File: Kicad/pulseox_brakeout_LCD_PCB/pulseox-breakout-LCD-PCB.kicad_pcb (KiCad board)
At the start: 2 copper layers, 47.4 x 44.4 mm, 20 parts, among them CON1 P3, P1 Header 8, P2 Header 2

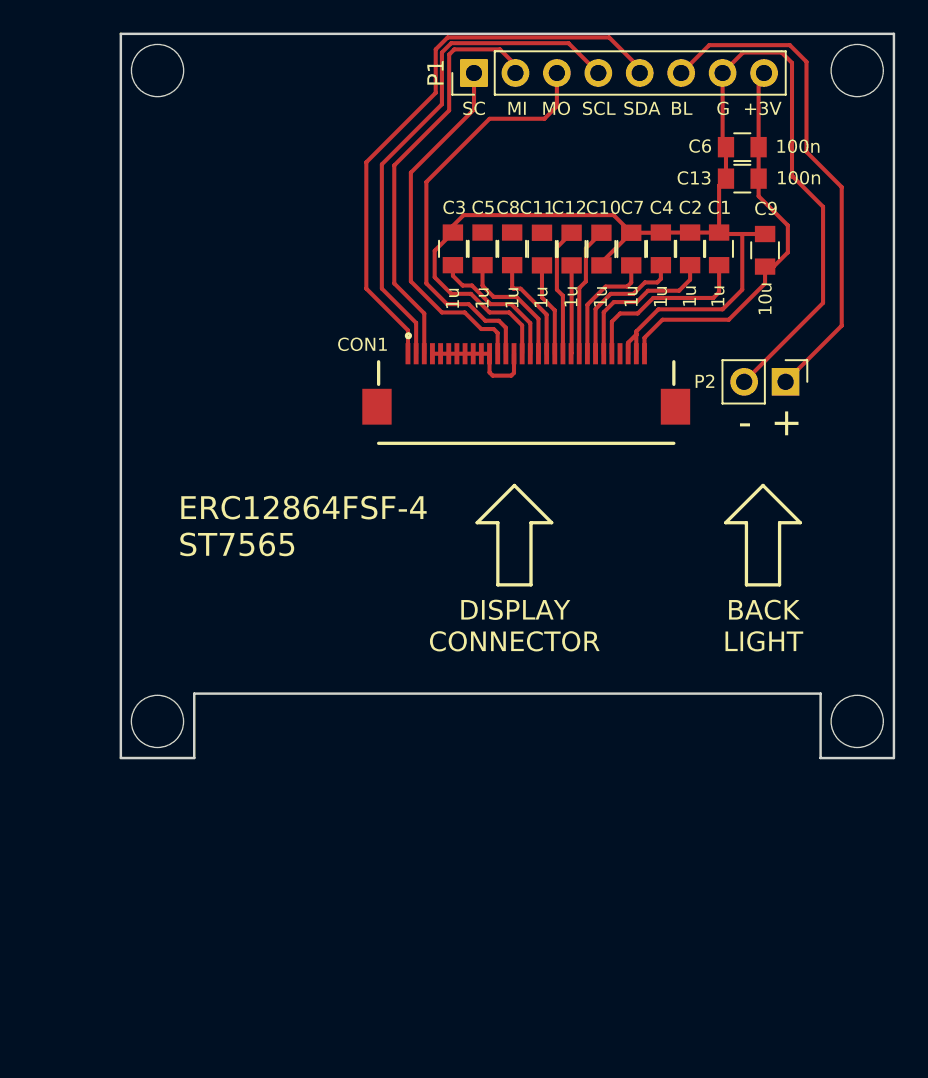
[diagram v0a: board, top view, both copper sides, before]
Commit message: Added output PDF files from Kicad project
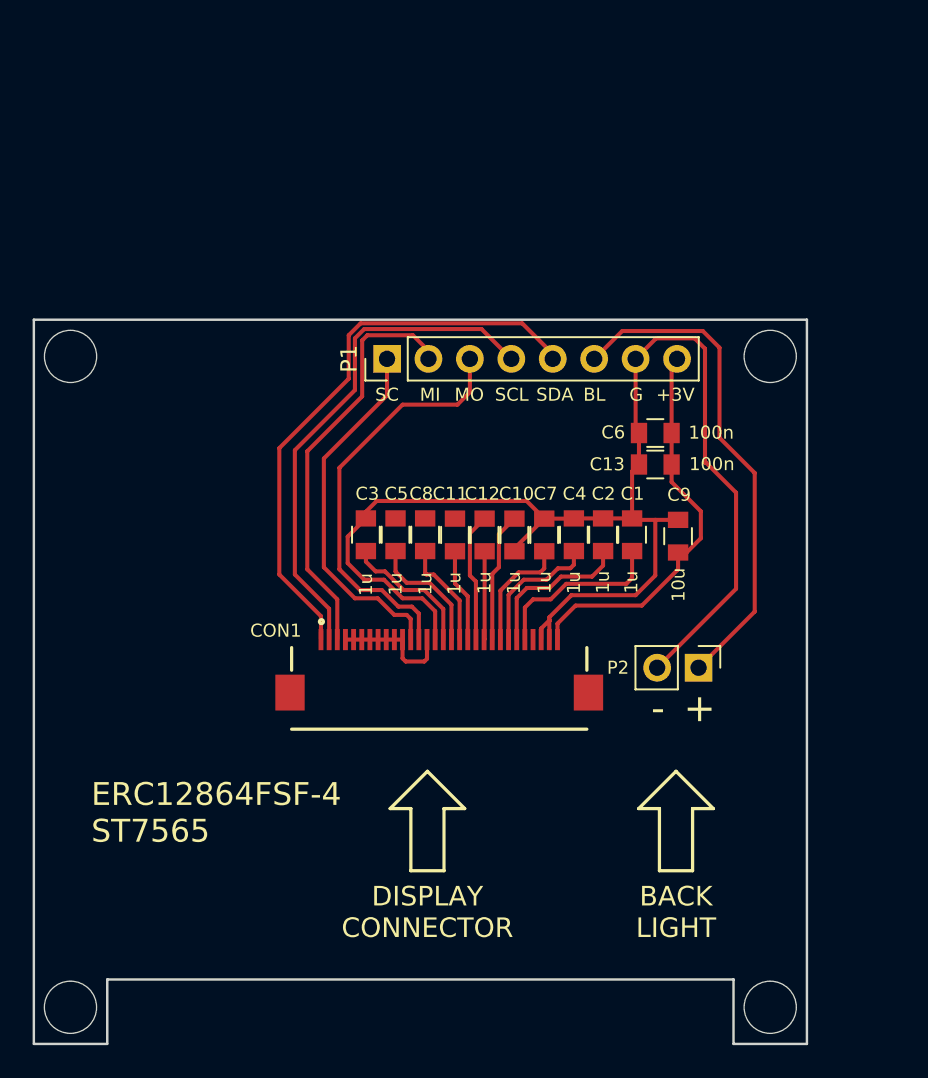
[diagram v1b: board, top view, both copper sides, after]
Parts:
- moved C6 18.3 mm to (167.4, 75.3)
- moved P2 18.3 mm to (170.0, 89.7)
- moved C2 18.3 mm to (164.2, 81.5)
- moved C3 18.3 mm to (149.6, 81.5)
- moved C4 18.3 mm to (162.4, 81.5)
- moved C5 18.3 mm to (151.5, 81.5)
- moved C8 18.3 mm to (153.3, 81.5)
- moved C10 18.3 mm to (158.8, 81.5)
- moved C11 18.3 mm to (155.1, 81.5)
- moved C12 18.3 mm to (156.9, 81.5)
- moved C13 18.3 mm to (167.4, 77.2)
- moved C7 18.3 mm to (160.6, 81.5)
- moved C9 18.3 mm to (168.8, 81.6)
- moved MK1 18.3 mm to (131.5, 70.6)
- moved MK2 18.3 mm to (174.4, 70.6)
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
